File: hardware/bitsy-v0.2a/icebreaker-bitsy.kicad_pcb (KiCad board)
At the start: 4 copper layers, 38.1 x 17.8 mm, 95 parts, among them J1 Conn_01x01, J10 Conn_01x01, J11 Conn_01x01, J12 Conn_01x01, J13 Conn_01x01, J14 Jumper, J15 Jumper, J16 Jumper, J17 Jumper, J18 Jumper, J19 Jumper, J2 Conn_01x01, J20 Conn_01x01, J21 Conn_01x01, J22 Conn_01x01, J23 Conn_01x01, J24 Conn_01x01, J25 Conn_01x01, J26 Conn_01x01, J27 Conn_01x01, J28 Conn_01x01, J29 Conn_01x01, J3 Conn_01x01, J30 Conn_01x01, J31 Conn_01x01, J32 Conn_01x01, J33 Conn_01x01, J34 Conn_01x01, J35 Conn_01x01, J36 Conn_01x01, J37 Conn_01x01, J38 Jumper, J4 Conn_01x01, J41 Conn_01x01, J42 Conn_01x01, J43 Conn_01x01, J44 Conn_01x01, J45 Conn_01x01, J46 Conn_01x01, J47 Conn_01x01, J48 Conn_01x01, J49 Conn_01x01, J5 Conn_01x01, J6 Conn_01x01, J7 Conn_01x01, J8 Conn_01x01, J9 Conn_01x01, P1 USB_OTG, SW1 TACT, U1 USBLC6-2, U2 3.3V, U3 1V2, U5 W25Q, U6 ICE5LP4K-SG48, X1 12MHz

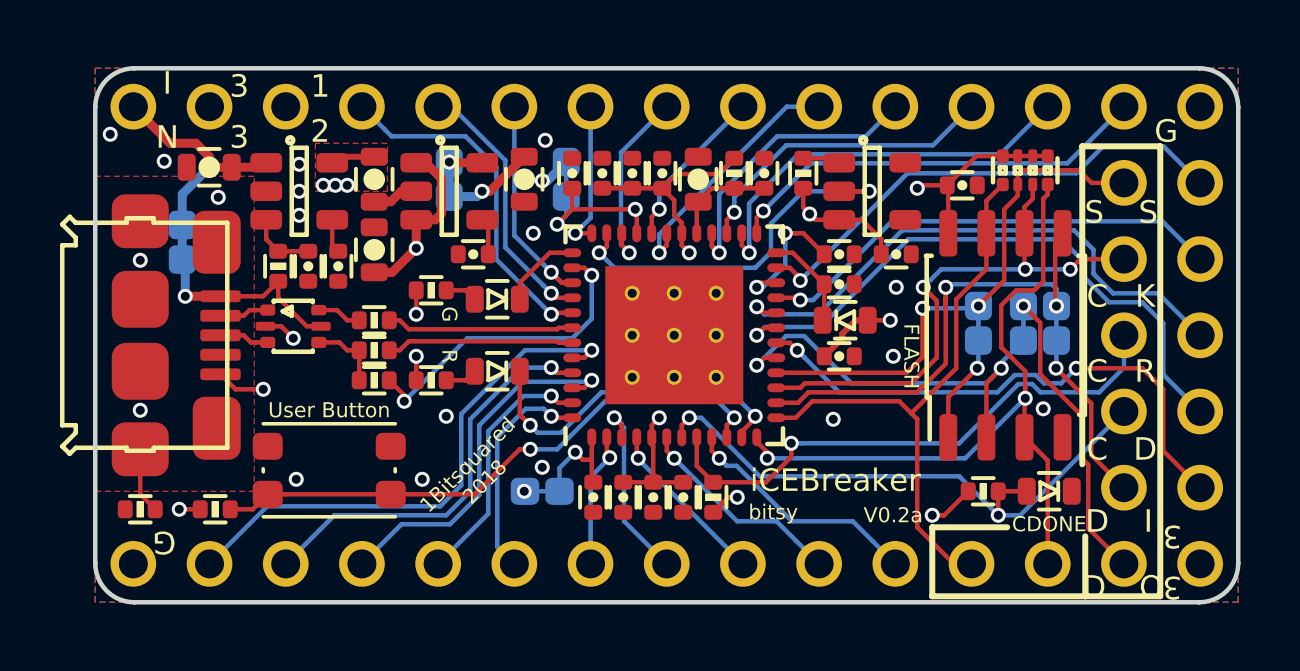
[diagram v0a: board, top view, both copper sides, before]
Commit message: Fixed #6 Oscillator pinout and schematic symbol.
Both bitsy and icebreaker.
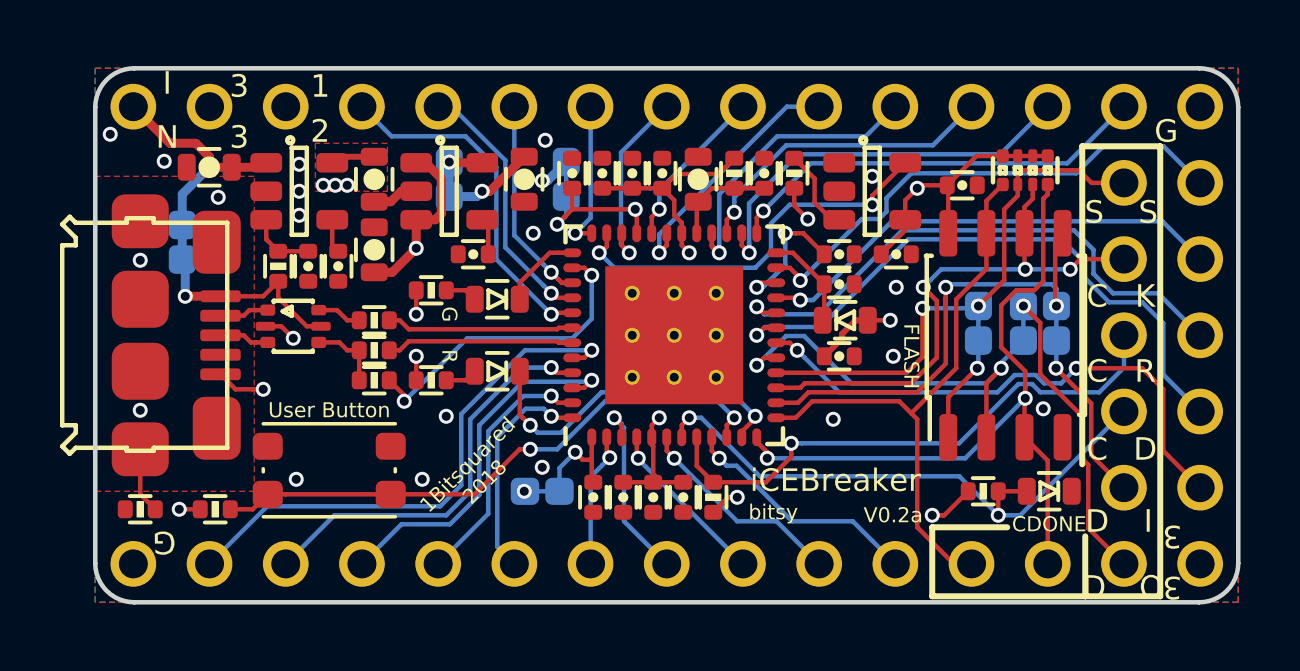
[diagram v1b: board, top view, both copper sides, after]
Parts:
- moved R7 0.30 mm to (53.3, 42.1)
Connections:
- X1 pad 1: Net-(R7-Pad2) -> GND
- X1 pad 2: /CLK -> Net-(X1-Pad2)
- X1 pad 3: +3V3 -> Net-(R7-Pad2)
- X1 pad 4: GND -> +3V3
- X1 pad 5: (no net) -> /CLK
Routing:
- net Net-(R7-Pad2): track 1.26 -> 2.82 mm
- net /CLK: track 12.6 -> 13.4 mm
- net GND: vias 18 -> 19
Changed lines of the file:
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@@
-(kicad_pcb (version 20171130) (host pcbnew 5.0.0-rc2-dev-unknown-2c85de3~62~ubuntu16.04.1)
+(kicad_pcb (version 20171130) (host pcbnew 5.0.0-rc2-dev-unknown-2da7199~62~ubuntu16.04.1)
   (general
     (thickness 1.6)
     (drawings 161)
-    (tracks 669)
+    (tracks 676)
     (zones 0)
     (modules 95)
-    (nets 60)
+    (nets 61)
   )
   (page A4)
@@
   (net 58 /iUD-)
   (net 59 /IOT_36B)
+  (net 60 "Net-(X1-Pad2)")
   (net_class Default "This is the default net class."
     (clearance 0.15)
@@
     (add_net "Net-(P1-Pad4)")
     (add_net "Net-(R7-Pad2)")
+    (add_net "Net-(X1-Pad2)")
   )
   (module pkl_jumpers:J_0603 (layer B.Cu)
@@
   )
   (module pkl_dipol:R_0402 (layer F.Cu)
-    (at 53.6 42.1 90)
+    (at 53.3 42.1 90)
     (descr "Resistor SMD 0402, reflow soldering")
     (tags "resistor 0402")
@@
     (fp_line (start 0.25 1.45) (end 0.25 -1.45) (layer F.SilkS) (width 0.15))
     (pad 1 smd roundrect (at 1.1 0.95) (size 1.06 0.65) (layers F.Cu F.Paste F.Mask)(roundrect_rratio 0.25)
-      (net 8 "Net-(R7-Pad2)"))
+      (net 7 GND))
     (pad 2 smd roundrect (at 1.1 0) (size 1.06 0.65) (layers F.Cu F.Paste F.Mask)(roundrect_rratio 0.25)
-      (net 29 /CLK))
+      (net 60 "Net-(X1-Pad2)"))
     (pad 3 smd roundrect (at 1.1 -0.95) (size 1.06 0.65) (layers F.Cu F.Paste F.Mask)(roundrect_rratio 0.25)
-      (net 2 +3V3))
+      (net 8 "Net-(R7-Pad2)"))
     (pad 4 smd roundrect (at -1.1 -0.95) (size 1.06 0.65) (layers F.Cu F.Paste F.Mask)(roundrect_rratio 0.25)
-      (net 7 GND))
-    (pad 5 smd roundrect (at -1.1 0.95) (size 1.06 0.65) (layers F.Cu F.Paste F.Mask)(roundrect_rratio 0.25))
+      (net 2 +3V3))
+    (pad 5 smd roundrect (at -1.1 0.95) (size 1.06 0.65) (layers F.Cu F.Paste F.Mask)(roundrect_rratio 0.25)
+      (net 29 /CLK))
     (model TO_SOT_Packages_SMD.3dshapes/SOT-23-5.wrl
       (at (xyz 0 0 0))
@@
   (segment (start 45.15 44.75) (end 45.45 44.75) (width 0.15) (layer F.Cu) (net 1))
   (segment (start 45.45 44.75) (end 45.9 44.75) (width 0.15) (layer F.Cu) (net 1))
+  (segment (start 53.3 42.6) (end 53.3 43.17501) (width 0.15) (layer F.Cu) (net 2))
+  (via (at 53.75 43.62501) (size 0.5) (drill 0.3) (layers F.Cu B.Cu) (net 2))
+  (segment (start 53.3 43.17501) (end 53.75 43.62501) (width 0.15) (layer F.Cu) (net 2))
+  (segment (start 57 43.65) (end 57 42.99999) (width 0.15) (layer F.Cu) (net 2))
+  (segment (start 57 42.99999) (end 57.39999 42.6) (width 0.15) (layer F.Cu) (net 2))
+  (segment (start 57 43.65) (end 57 44) (width 0.15) (layer F.Cu) (net 2))
+  (segment (start 57 44) (end 56.2 44.8) (width 0.15) (layer F.Cu) (net 2))
   (segment (start 52.7 45.249987) (end 52.05 45.899987) (width 0.15) (layer In2.Cu) (net 2))
   (segment (start 52.7 45.75) (end 52.199987 45.75) (width 0.15) (layer F.Cu) (net 2))
@@
   (segment (start 58.435 44.1) (end 58.435 42.535) (width 0.15) (layer F.Cu) (net 2))
   (segment (start 58.435 42.535) (end 58.4 42.5) (width 0.15) (layer F.Cu) (net 2))
-  (segment (start 56.2 44.8) (end 56.2 44.3) (width 0.15) (layer F.Cu) (net 2))
-  (segment (start 56.2 44.3) (end 55.55 43.65) (width 0.15) (layer F.Cu) (net 2))
-  (segment (start 55.55 43.65) (end 54.8 43.65) (width 0.15) (layer F.Cu) (net 2))
-  (segment (start 53.6 43.244098) (end 53.813682 43.45778) (width 0.15) (layer F.Cu) (net 2))
-  (segment (start 54.005902 43.65) (end 53.813682 43.45778) (width 0.15) (layer F.Cu) (net 2))
-  (segment (start 53.6 42.6) (end 53.6 43.244098) (width 0.15) (layer F.Cu) (net 2))
-  (via (at 53.813682 43.45778) (size 0.5) (drill 0.3) (layers F.Cu B.Cu) (net 2))
-  (segment (start 54.8 43.65) (end 54.005902 43.65) (width 0.15) (layer F.Cu) (net 2))
   (segment (start 55.75 47) (end 56.5 47) (width 0.15) (layer F.Cu) (net 2))
   (via (at 56.5 47) (size 0.5) (drill 0.3) (layers F.Cu B.Cu) (net 2))
@@
   (segment (start 44.250001 50.250001) (end 44.5 50.5) (width 0.15) (layer F.Cu) (net 6))
   (via (at 44.5 50.5) (size 0.5) (drill 0.3) (layers F.Cu B.Cu) (net 6))
+  (via (at 55.9 42.2) (size 0.5) (drill 0.3) (layers F.Cu B.Cu) (net 7))
   (via (at 36.8 43.49999) (size 0.5) (drill 0.3) (layers F.Cu B.Cu) (net 7))
   (via (at 61.6 49.95) (size 0.5) (drill 0.3) (layers F.Cu B.Cu) (net 7))
@@
   (via (at 30.5 40.8) (size 0.5) (drill 0.3) (layers F.Cu B.Cu) (net 7))
   (via (at 32.3 41.7) (size 0.5) (drill 0.3) (layers F.Cu B.Cu) (net 7))
-  (segment (start 53.6 41.6) (end 54.65 41.6) (width 0.15) (layer F.Cu) (net 8))
-  (segment (start 54.65 41.6) (end 54.8 41.75) (width 0.15) (layer F.Cu) (net 8))
+  (segment (start 53.978002 42.278002) (end 53.978002 43.074998) (width 0.15) (layer F.Cu) (net 8))
+  (segment (start 53.3 41.6) (end 53.978002 42.278002) (width 0.15) (layer F.Cu) (net 8))
+  (segment (start 53.978002 43.074998) (end 54.553004 43.65) (width 0.15) (layer F.Cu) (net 8))
+  (segment (start 54.553004 43.65) (end 54.8 43.65) (width 0.15) (layer F.Cu) (net 8))
   (segment (start 37.9 43.65) (end 37.9 44.5) (width 0.15) (layer F.Cu) (net 9))
   (segment (start 37.9 44.5) (end 38.1 44.7) (width 0.15) (layer F.Cu) (net 9))
@@
   (segment (start 35.7 43.65) (end 35.7 44.3) (width 0.15) (layer F.Cu) (net 28))
   (segment (start 35.7 44.3) (end 36.1 44.7) (width 0.15) (layer F.Cu) (net 28))
-  (segment (start 52.524998 44.725002) (end 52 45.25) (width 0.15) (layer B.Cu) (net 29))
-  (segment (start 52.524998 43.771998) (end 52.524998 44.725002) (width 0.15) (layer B.Cu) (net 29))
-  (segment (start 53.596996 42.7) (end 52.524998 43.771998) (width 0.15) (layer B.Cu) (net 29))
-  (segment (start 55.8 42.7) (end 53.596996 42.7) (width 0.15) (layer B.Cu) (net 29))
-  (segment (start 52 45.25) (end 47.3 45.25) (width 0.15) (layer B.Cu) (net 29))
-  (segment (start 47.3 45.25) (end 46.8 44.75) (width 0.15) (layer B.Cu) (net 29))
+  (via (at 55.9 43.15) (size 0.5) (drill 0.3) (layers F.Cu B.Cu) (net 29))
+  (segment (start 57 41.75) (end 55.9 42.85) (width 0.15) (layer F.Cu) (net 29))
+  (segment (start 52.524998 44.725002) (end 52.524998 43.771998) (width 0.15) (layer B.Cu) (net 29))
+  (segment (start 46.8 44.75) (end 47.3 45.25) (width 0.15) (layer B.Cu) (net 29))
+  (segment (start 47.3 45.25) (end 52 45.25) (width 0.15) (layer B.Cu) (net 29))
+  (segment (start 55.9 42.85) (end 55.9 43.15) (width 0.15) (layer F.Cu) (net 29))
+  (segment (start 52 45.25) (end 52.524998 44.725002) (width 0.15) (layer B.Cu) (net 29))
+  (segment (start 53.146996 43.15) (end 55.9 43.15) (width 0.15) (layer B.Cu) (net 29))
+  (segment (start 52.524998 43.771998) (end 53.146996 43.15) (width 0.15) (layer B.Cu) (net 29))
   (via (at 46.8 44.75) (size 0.5) (drill 0.3) (layers F.Cu B.Cu) (net 29))
   (segment (start 47.05 44.55) (end 46.85 44.75) (width 0.15) (layer F.Cu) (net 29))
   (segment (start 46.85 44.75) (end 46.8 44.75) (width 0.15) (layer F.Cu) (net 29))
   (segment (start 47.05 44.1) (end 47.05 44.55) (width 0.15) (layer F.Cu) (net 29))
-  (segment (start 55.8 42.7) (end 54.8 42.7) (width 0.15) (layer F.Cu) (net 29))
-  (via (at 55.8 42.7) (size 0.5) (drill 0.3) (layers F.Cu B.Cu) (net 29))
   (segment (start 40.45 47.3) (end 45.4 47.3) (width 0.15) (layer F.Cu) (net 30))
   (segment (start 45.4 47.3) (end 45.45 47.25) (width 0.15) (layer F.Cu) (net 30))
@@
   (segment (start 49.05 51.35) (end 49.3 51.6) (width 0.15) (layer F.Cu) (net 44))
   (via (at 49.3 51.6) (size 0.5) (drill 0.3) (layers F.Cu B.Cu) (net 44))
+  (segment (start 57.203004 42.1) (end 56.375002 42.928002) (width 0.15) (layer B.Cu) (net 48))
+  (segment (start 56.375002 43.378002) (end 56.128002 43.625002) (width 0.15) (layer B.Cu) (net 48))
+  (segment (start 66.83 42.42) (end 65.61 41.2) (width 0.15) (layer B.Cu) (net 48))
+  (segment (start 62.7 42.1) (end 57.203004 42.1) (width 0.15) (layer B.Cu) (net 48))
+  (segment (start 65.61 41.2) (end 63.6 41.2) (width 0.15) (layer B.Cu) (net 48))
+  (segment (start 55.549975 43.625002) (end 53.749999 45.424978) (width 0.15) (layer B.Cu) (net 48))
+  (segment (start 56.375002 42.928002) (end 56.375002 43.378002) (width 0.15) (layer B.Cu) (net 48))
+  (segment (start 56.128002 43.625002) (end 55.549975 43.625002) (width 0.15) (layer B.Cu) (net 48))
+  (segment (start 63.6 41.2) (end 62.7 42.1) (width 0.15) (layer B.Cu) (net 48))
+  (segment (start 53.749999 45.424978) (end 53.5 45.674977) (width 0.15) (layer B.Cu) (net 48))
   (segment (start 62.402966 41.767034) (end 53.858196 41.767034) (width 0.15) (layer B.Cu) (net 59))
   (segment (start 52.05 43.57523) (end 52.269418 43.355812) (width 0.15) (layer F.Cu) (net 59))
@@
   (segment (start 47.55 44.1) (end 47.55 44.5) (width 0.15) (layer F.Cu) (net 46))
   (segment (start 53.5 45.6) (end 53.5 45.674977) (width 0.15) (layer F.Cu) (net 48))
-  (segment (start 66.83 42.42) (end 65.61 41.2) (width 0.15) (layer B.Cu) (net 48))
   (segment (start 52.7 45.25) (end 53.15 45.25) (width 0.15) (layer F.Cu) (net 48))
-  (segment (start 63.6 41.2) (end 62.7 42.1) (width 0.15) (layer B.Cu) (net 48))
-  (segment (start 53.749999 45.424978) (end 53.5 45.674977) (width 0.15) (layer B.Cu) (net 48))
   (segment (start 53.15 45.25) (end 53.5 45.6) (width 0.15) (layer F.Cu) (net 48))
-  (segment (start 65.61 41.2) (end 63.6 41.2) (width 0.15) (layer B.Cu) (net 48))
-  (segment (start 62.7 42.1) (end 57.074977 42.1) (width 0.15) (layer B.Cu) (net 48))
   (via (at 53.5 45.674977) (size 0.5) (drill 0.3) (layers F.Cu B.Cu) (net 48))
-  (segment (start 57.074977 42.1) (end 53.749999 45.424978) (width 0.15) (layer B.Cu) (net 48))
   (segment (start 51.8 44.446447) (end 51.8 44.749994) (width 0.15) (layer B.Cu) (net 49))
   (segment (start 51.8 44.749994) (end 51.800006 44.75) (width 0.15) (layer B.Cu) (net 49))
